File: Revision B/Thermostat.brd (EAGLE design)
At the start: 50.8 x 50.8 mm, 27 parts

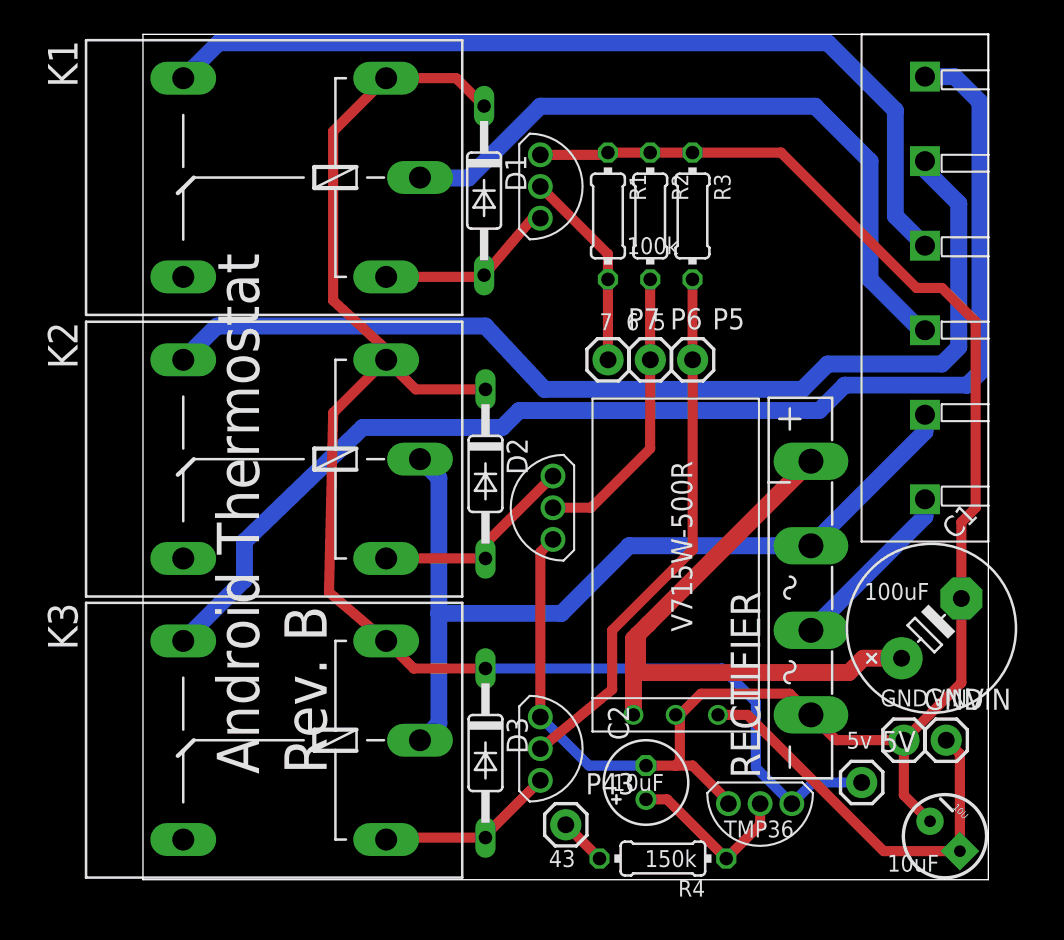
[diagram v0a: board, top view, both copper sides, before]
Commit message: Moved Rectifier
On the third print the bridge rectifier was too close to the 100uf
capacitor.  I moved it slightly and had to move the regulator and diodes
as well.
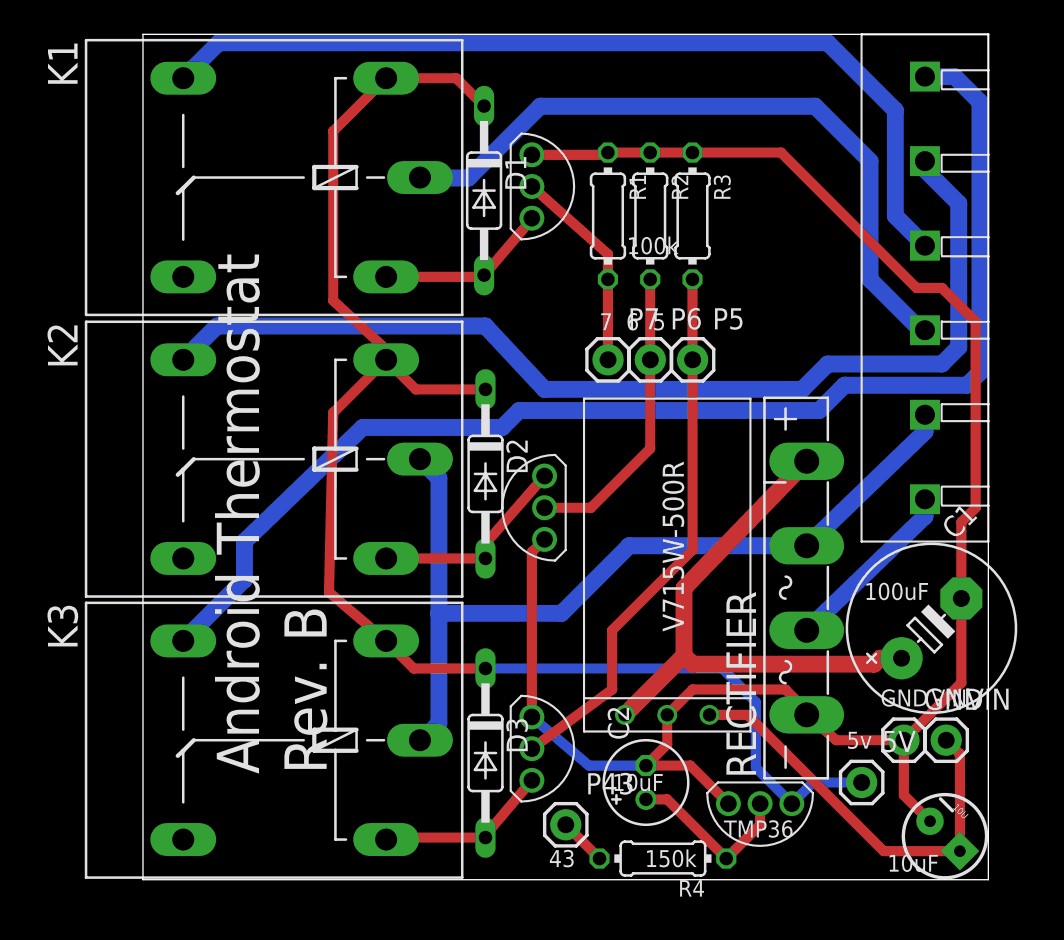
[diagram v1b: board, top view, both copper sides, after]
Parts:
- moved U$4 0.51 mm to (23.4, 7.87)
- moved U$5 0.51 mm to (24.1, 22.4)
- moved U$6 0.51 mm to (23.4, 41.7)
- moved U$2 0.51 mm to (31.5, 9.91)
- moved RECTIFIER 0.25 mm to (39.9, 17.5)
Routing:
- net N$24: track 38.2 -> 33.1 mm
- net GND: track 106.0 -> 108.3 mm
- net N$2: track 17.5 -> 18.0 mm
- net N$10: track 24.9 -> 25.4 mm

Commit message: Moved Temperature Sensor
It was too close to the switching regulator which is putting out a lot
of heat.
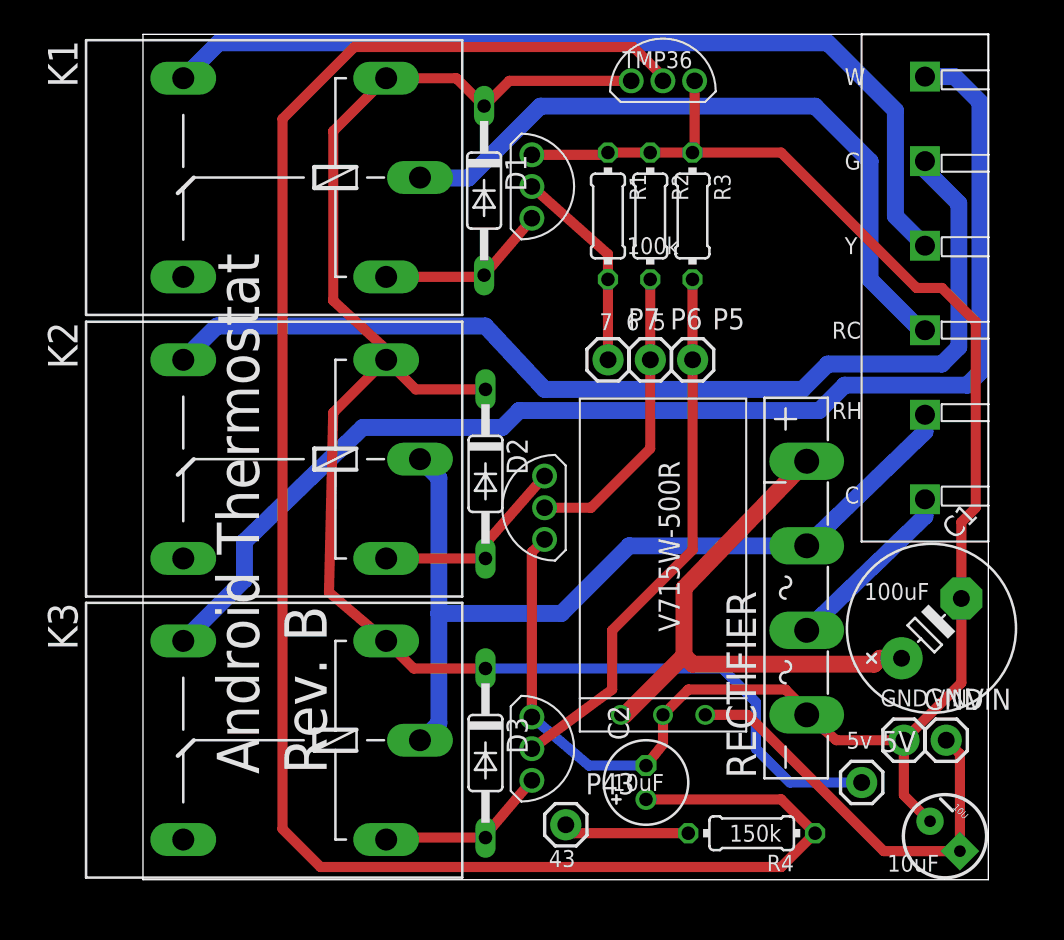
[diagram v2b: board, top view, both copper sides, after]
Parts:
- moved U$1 43.8 mm to (31.2, 48.0), turned to 90 degrees
- moved R4 5.55 mm to (36.6, 2.79)
- moved U$2 0.25 mm to (31.2, 9.91)
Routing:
- net N$4: track 10.4 -> 113.1 mm
- net +5V: track 88.2 -> 95.9 mm
- net N$5: track 2.87 -> 7.57 mm
- net GND: track 108.3 -> 106.9 mm
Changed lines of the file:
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@@
 <text x="49.8983" y="42.672" size="1.016" layer="122" font="vector" rot="MR0">G</text>
 <text x="49.8983" y="47.498" size="1.016" layer="122" font="vector" rot="MR0">W</text>
-<text x="34.9123" y="2.54" size="1.016" layer="121" font="vector">TMP36</text>
+<text x="28.8163" y="48.768" size="1.016" layer="121" font="vector">TMP36</text>
 <text x="43.335215625" y="16.81400625" size="1.016" layer="121" font="vector">100uF</text>
 <text x="44.723190625" y="0.483609375" size="1.016" layer="121" font="vector">10uF</text>
@@
 <text x="4.572" y="6.096" size="2.54" layer="122" font="vector" rot="MR90">Rev. B</text>
 <text x="28.194" y="5.334" size="1.016" layer="121" font="vector">10uF</text>
-<text x="33.274" y="1.778" size="1.016" layer="121" font="vector" rot="R180">150k</text>
+<text x="38.354" y="3.302" size="1.016" layer="121" font="vector" rot="R180">150k</text>
 <text x="27.432" y="33.02" size="1.016" layer="121" font="vector">7  6  5</text>
 <text x="24.384" y="0.762" size="1.016" layer="121" font="vector">43</text>
+<text x="42.164" y="47.752" size="1.016" layer="121" font="vector">W</text>
+<text x="42.164" y="42.672" size="1.016" layer="121" font="vector">G</text>
+<text x="42.164" y="37.592" size="1.016" layer="121" font="vector">Y</text>
+<text x="41.402" y="32.512" size="1.016" layer="121" font="vector">RC</text>
+<text x="41.402" y="27.686" size="1.016" layer="121" font="vector">RH</text>
+<text x="42.164" y="22.606" size="1.016" layer="121" font="vector">C</text>
 </plain>
 <attributes>
@@
 <element name="P7" library="SparkFun-Connectors" package="1X01" value="" x="27.9463" y="31.242"/>
 <element name="VIN" library="SparkFun-Connectors" package="1X01" value="" x="48.2663" y="8.382"/>
-<element name="U$2" library="android-thermostat" package="SWITCHINGREGULATOR" value="V715W-500R" x="31.5023" y="9.906" rot="R90"/>
+<element name="U$2" library="android-thermostat" package="SWITCHINGREGULATOR" value="V715W-500R" x="31.2483" y="9.906" rot="R90"/>
 <element name="K1" library="relay" package="G5LE" value="" x="7.1183" y="42.19448125" rot="R180">
 <attribute name="OC_NEWARK" value="unknown" x="7.1183" y="42.19448125" size="1.778" layer="27" rot="R180" display="off"/>
@@
 <element name="C2" library="rcl" package="E2-5" value="" x="30.226" y="5.842" rot="R90"/>
 <element name="U$3" library="android-thermostat" package="PHOENIX_E_5MM_6PIN" value="PHOENIX-651-1935200" x="46.99" y="35.56"/>
-<element name="U$1" library="android-thermostat" package="TMP36" value="TMP36" x="37.084" y="4.572" rot="R270"/>
+<element name="U$1" library="android-thermostat" package="TMP36" value="TMP36" x="31.242" y="48.006" rot="R90"/>
 <element name="U$4" library="android-thermostat" package="TRANSISTOR" value="TRANSISTOR" x="23.368" y="7.874"/>
 <element name="U$5" library="android-thermostat" package="TRANSISTOR" value="TRANSISTOR" x="24.13" y="22.352" rot="R180"/>
 <element name="U$6" library="android-thermostat" package="TRANSISTOR" value="TRANSISTOR" x="23.368" y="41.656"/>
-<element name="R4" library="rcl" package="0204/7" value="" x="31.242" y="1.27" rot="R180"/>
+<element name="R4" library="rcl" package="0204/7" value="" x="36.576" y="2.794" rot="R180"/>
 <element name="C1" library="rcl" package="E5-10,5" value="" x="47.380028125" y="15.103975" rot="R45"/>
 </elements>
@@
 <wire x1="39.8843" y1="9.906" x2="40.132" y2="9.906" width="0.6096" layer="1"/>
 <wire x1="40.132" y1="9.906" x2="38.608" y2="11.43" width="0.6096" layer="1"/>
-<wire x1="38.608" y1="11.43" x2="33.0263" y2="11.43" width="0.6096" layer="1"/>
-<wire x1="33.0263" y1="11.43" x2="31.5023" y2="9.906" width="0.6096" layer="1"/>
-<wire x1="31.5023" y1="9.906" x2="31.5023" y2="8.1343" width="0.6096" layer="1"/>
-<wire x1="31.5023" y1="8.1343" x2="30.226" y2="6.858" width="0.6096" layer="1"/>
-<wire x1="30.226" y1="6.858" x2="32.893" y2="6.858" width="0.6096" layer="1"/>
-<wire x1="32.893" y1="6.858" x2="35.179" y2="4.572" width="0.6096" layer="1"/>
+<wire x1="38.608" y1="11.43" x2="32.7723" y2="11.43" width="0.6096" layer="1"/>
+<wire x1="32.7723" y1="11.43" x2="31.2483" y2="9.906" width="0.6096" layer="1"/>
+<wire x1="31.2483" y1="9.906" x2="31.2483" y2="8.1343" width="0.6096" layer="1"/>
+<wire x1="31.2483" y1="8.1343" x2="30.226" y2="6.858" width="0.6096" layer="1"/>
+<wire x1="33.147" y1="48.006" x2="33.147" y2="43.8213" width="0.6096" layer="1"/>
+<wire x1="33.147" y1="43.8213" x2="33.02" y2="43.6943" width="0.6096" layer="1"/>
 </signal>
 <signal name="N$2">
@@
 <contactref element="5V" pad="1"/>
 <contactref element="U$1" pad="VC1"/>
-<wire x1="43.1863" y1="5.842" x2="40.259" y2="5.842" width="0.6096" layer="16"/>
-<wire x1="40.259" y1="5.842" x2="38.989" y2="4.572" width="0.6096" layer="16"/>
 <wire x1="20.5803" y1="12.692" x2="34.806" y2="12.692" width="0.6096" layer="16"/>
 <wire x1="34.806" y1="12.692" x2="36.83" y2="10.668" width="0.6096" layer="16"/>
-<wire x1="36.83" y1="10.668" x2="36.83" y2="6.731" width="0.6096" layer="16"/>
-<wire x1="36.83" y1="6.731" x2="38.989" y2="4.572" width="0.6096" layer="16"/>
+<wire x1="36.83" y1="10.668" x2="36.83" y2="7.874" width="0.6096" layer="16"/>
+<wire x1="36.83" y1="7.874" x2="38.862" y2="5.842" width="0.6096" layer="16"/>
+<wire x1="38.862" y1="5.842" x2="43.1863" y2="5.842" width="0.6096" layer="16"/>
+<wire x1="29.337" y1="48.006" x2="22.012859375" y2="48.006" width="0.6096" layer="1"/>
+<wire x1="22.012859375" y1="48.006" x2="20.496478125" y2="46.48961875" width="0.6096" layer="1"/>
 </signal>
 <signal name="N$3">
@@
 <wire x1="49.089928125" y1="1.716365625" x2="44.511634375" y2="1.716365625" width="0.6096" layer="1"/>
 <wire x1="44.511634375" y1="1.716365625" x2="36.322" y2="9.906" width="0.6096" layer="1"/>
-<wire x1="36.322" y1="9.906" x2="34.0423" y2="9.906" width="0.6096" layer="1"/>
+<wire x1="36.322" y1="9.906" x2="33.7883" y2="9.906" width="0.6096" layer="1"/>
 </signal>
 <signal name="N$24">
@@
 <contactref element="RECTIFIER" pad="+"/>
 <contactref element="C1" pad="+"/>
-<wire x1="28.9623" y1="9.906" x2="28.9623" y2="9.9123" width="1.016" layer="1"/>
+<wire x1="28.7083" y1="9.906" x2="28.9623" y2="9.9123" width="1.016" layer="1"/>
 <wire x1="28.9623" y1="9.9123" x2="32.512" y2="13.462" width="1.016" layer="1"/>
 <wire x1="32.512" y1="13.462" x2="32.512" y2="17.5197" width="1.016" layer="1"/>
@@
 <contactref element="U$1" pad="OUT2"/>
 <contactref element="R4" pad="1"/>
-<wire x1="30.226" y1="4.826" x2="31.496" y2="4.826" width="0.6096" layer="1"/>
-<wire x1="31.496" y1="4.826" x2="35.052" y2="1.27" width="0.6096" layer="1"/>
-<wire x1="37.084" y1="4.572" x2="37.084" y2="3.302" width="0.6096" layer="1"/>
-<wire x1="37.084" y1="3.302" x2="35.052" y2="1.27" width="0.6096" layer="1"/>
+<wire x1="30.226" y1="4.826" x2="38.354" y2="4.826" width="0.6096" layer="1"/>
+<wire x1="38.354" y1="4.826" x2="40.386" y2="2.794" width="0.6096" layer="1"/>
+<wire x1="31.242" y1="48.006" x2="31.242" y2="48.26" width="0.6096" layer="1"/>
+<wire x1="31.242" y1="48.26" x2="29.464" y2="50.038" width="0.6096" layer="1"/>
+<wire x1="29.464" y1="50.038" x2="12.7" y2="50.038" width="0.6096" layer="1"/>
+<wire x1="12.7" y1="50.038" x2="8.382" y2="45.72" width="0.6096" layer="1"/>
+<wire x1="8.382" y1="45.72" x2="8.382" y2="3.048" width="0.6096" layer="1"/>
+<wire x1="8.382" y1="3.048" x2="10.668" y2="0.762" width="0.6096" layer="1"/>
+<wire x1="10.668" y1="0.762" x2="38.354" y2="0.762" width="0.6096" layer="1"/>
+<wire x1="38.354" y1="0.762" x2="40.386" y2="2.794" width="0.6096" layer="1"/>
 </signal>
 <signal name="N$5">
 <contactref element="P43" pad="1"/>
 <contactref element="R4" pad="2"/>
-<wire x1="27.432" y1="1.27" x2="27.432" y2="1.2763" width="0.6096" layer="1"/>
-<wire x1="27.432" y1="1.2763" x2="25.4063" y2="3.302" width="0.6096" layer="1"/>
+<wire x1="32.766" y1="2.794" x2="25.9143" y2="2.794" width="0.6096" layer="1"/>
+<wire x1="25.9143" y1="2.794" x2="25.4063" y2="3.302" width="0.6096" layer="1"/>
 </signal>
 <signal name="N$9">
